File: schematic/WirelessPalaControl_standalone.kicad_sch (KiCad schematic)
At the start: 27 parts, among them J1 6P4C, J2 MCU UART, J3 WeMos_mini_Hat_Left, J4 WeMos_mini_Hat_Right, J5 RJ11 - Direct Link, Q1 AO3400A, Q2 AO3400A, U1 AMS1117-3.3

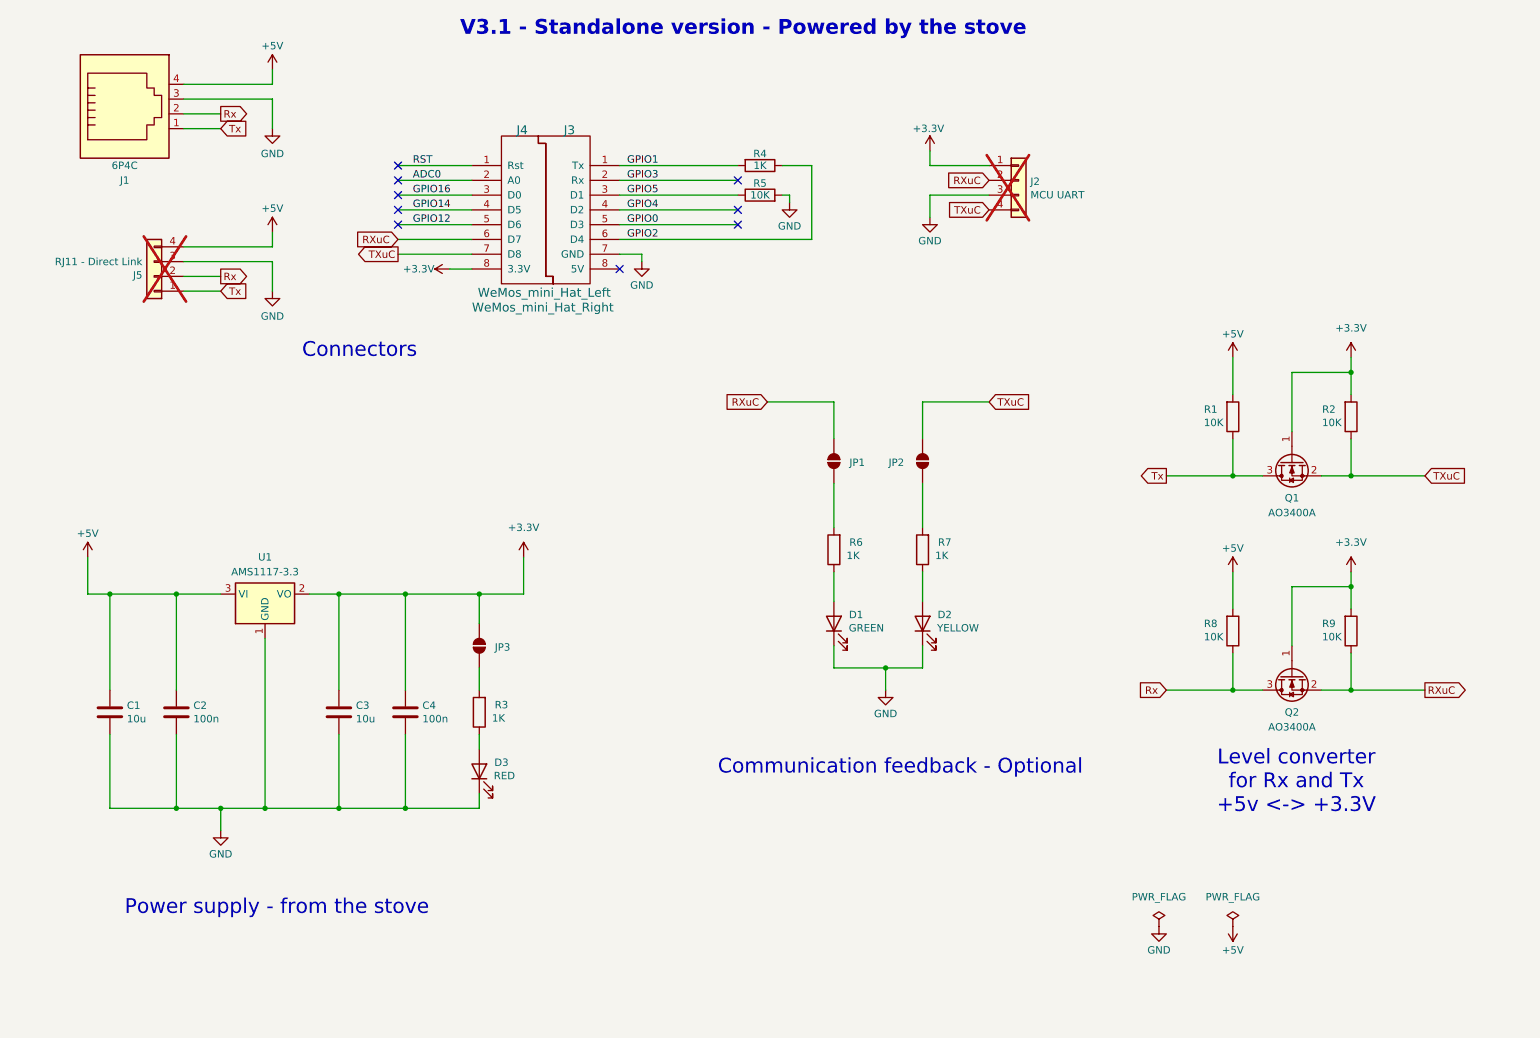
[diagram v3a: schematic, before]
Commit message: feat(hw): Cleanup schematic
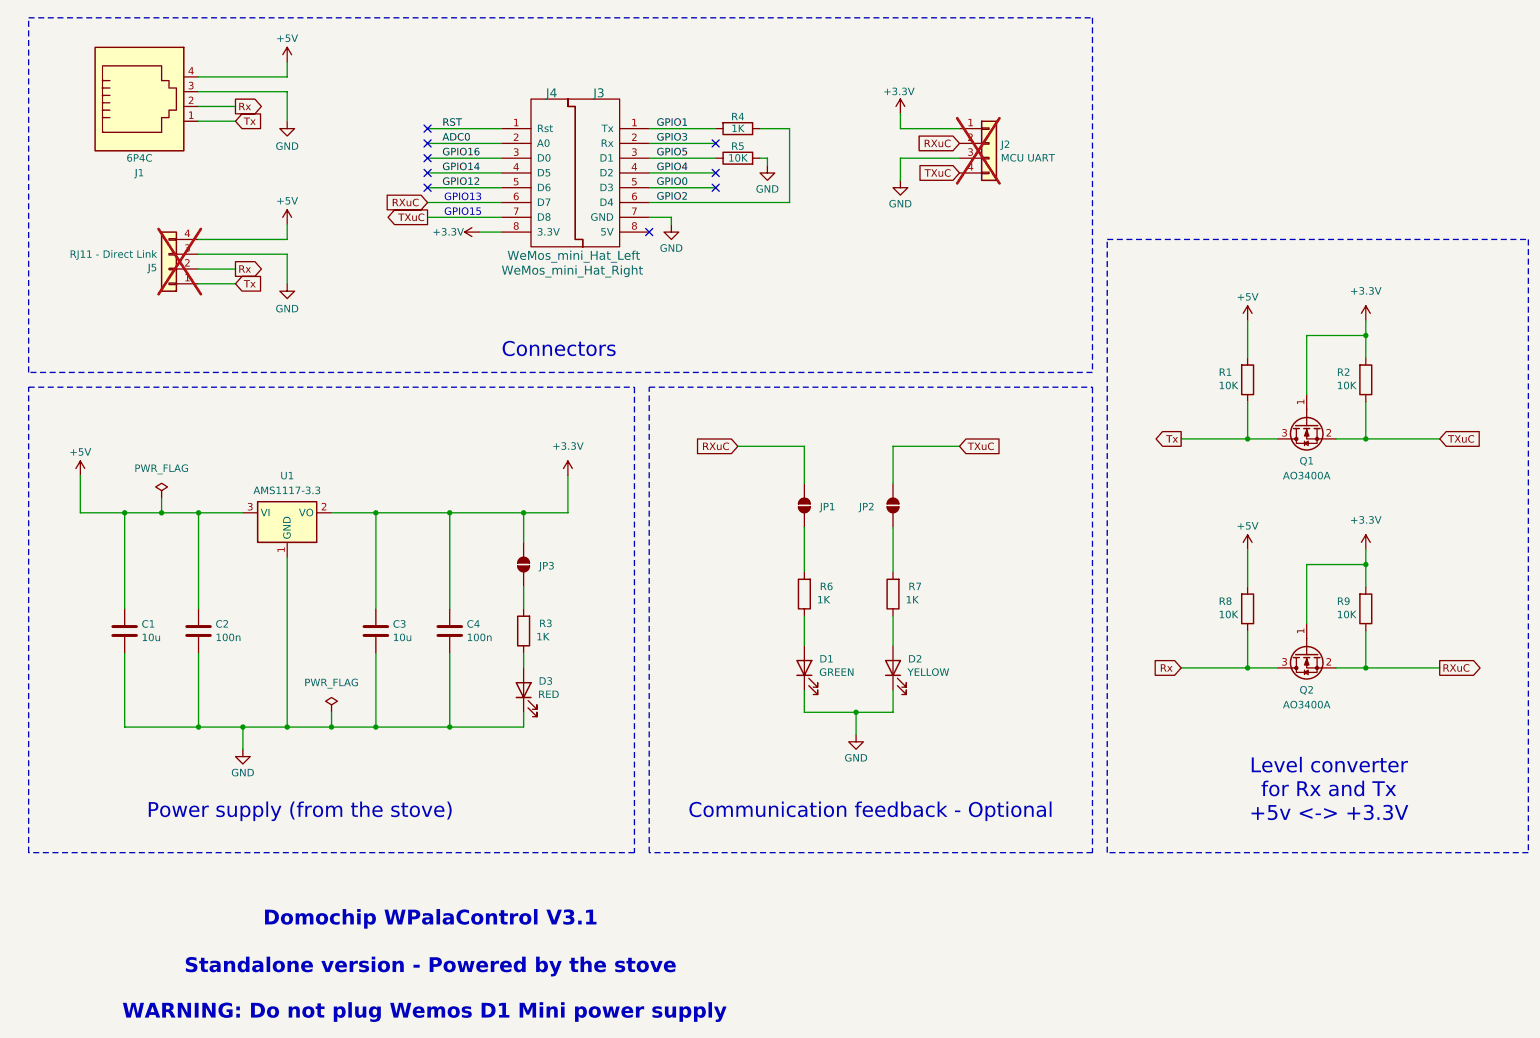
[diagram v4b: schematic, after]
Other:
- note added: "Domochip WPalaControl V3.1 Standalone version - Powered by the stove"
- note added: "GPIO13"
- note added: "GPIO15"
- note added: "Power supply (from the stove)"
- note added: "WARNING: Do not plug Wemos D1 Mini power supply"
- note removed: "Power supply - from the stove"
- note removed: "V3.1 - Standalone version - Powered by the stove"
- company: (none) -> Designed by Domochip and X@v
- title: (none) -> WPalaControl
- moved on the sheet: C1, C2, C3, C4, D1, D2, D3, J1, J2, J3, J4, J5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

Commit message: feat(hw): draft - Use D1 mini LDO
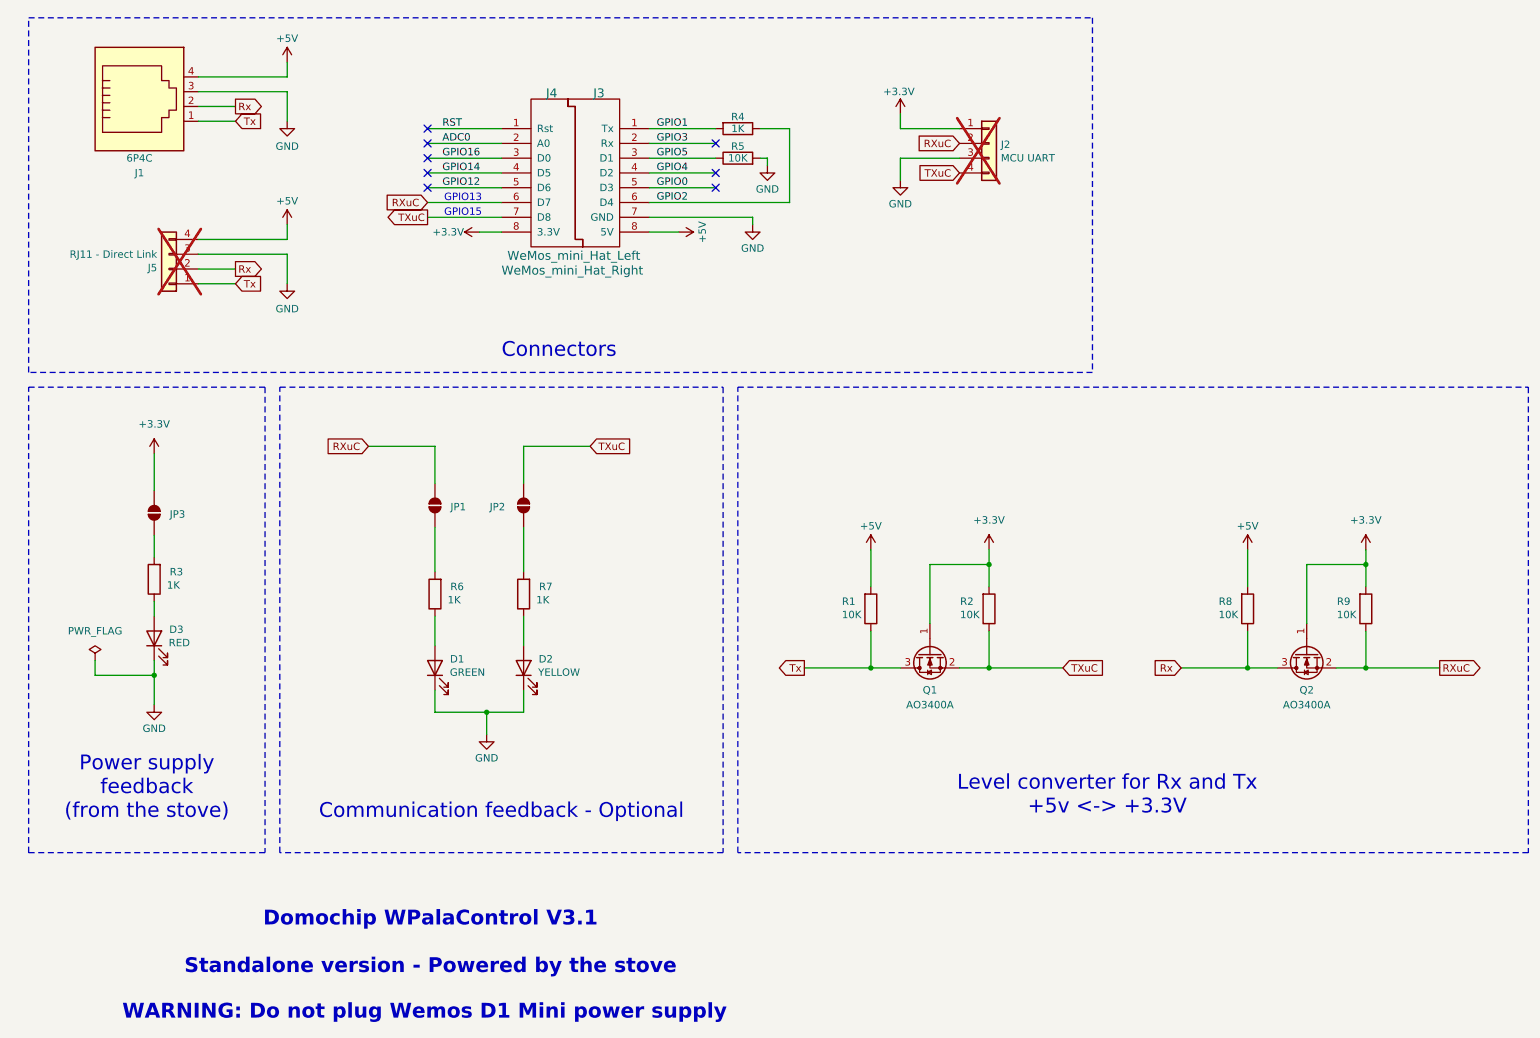
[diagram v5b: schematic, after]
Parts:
- removed C1, C3: 10u, Capacitor_SMD:C_0805_2012Metric_Pad1.18x1.45mm_HandSolder, symbol Device:C
- removed C2, C4: 100n, Capacitor_SMD:C_0805_2012Metric_Pad1.18x1.45mm_HandSolder, symbol Device:C
- removed U1: AMS1117-3.3, Package_TO_SOT_SMD:SOT-223-3_TabPin2, symbol Regulator_Linear:AMS1117-3.3
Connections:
- net +5V: now also J3.8 (5V)
- no-connect marks 9 -> 8
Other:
- note added: "Power supply feedback (from the stove)"
- note removed: "Power supply (from the stove)"
- moved on the sheet: D1, D2, D3, JP1, JP2, JP3, Q1, R1, R2, R3, R6, R7
